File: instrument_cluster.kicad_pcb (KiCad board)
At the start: 2 copper layers, 99.1 x 45.7 mm, 86 parts, among them J1 Conn_02x16_Top_Bottom, J2 Conn_02x16_Top_Bottom, J3 USB mini-B SMD, J4 NOT_FITTED_SWD_Conn_01x04_Male, J5 54819-0572, J6 NOT_FITTED_SWD_Conn_01x04_Male, U1 LM2575S-5.0_NOPB, U10 74HC4050D, U11 TJA1040T, U12 TJA1040T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

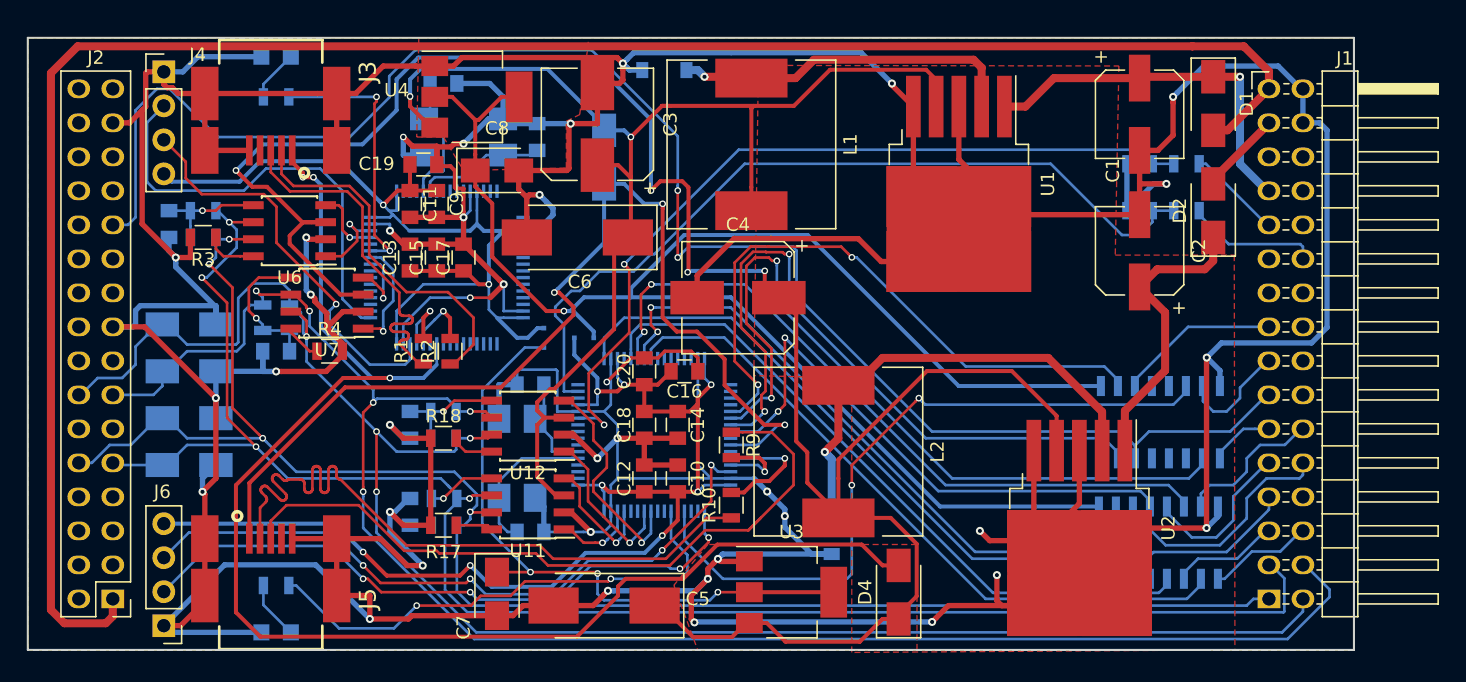
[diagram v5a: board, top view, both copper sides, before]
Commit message: fix USB footprint
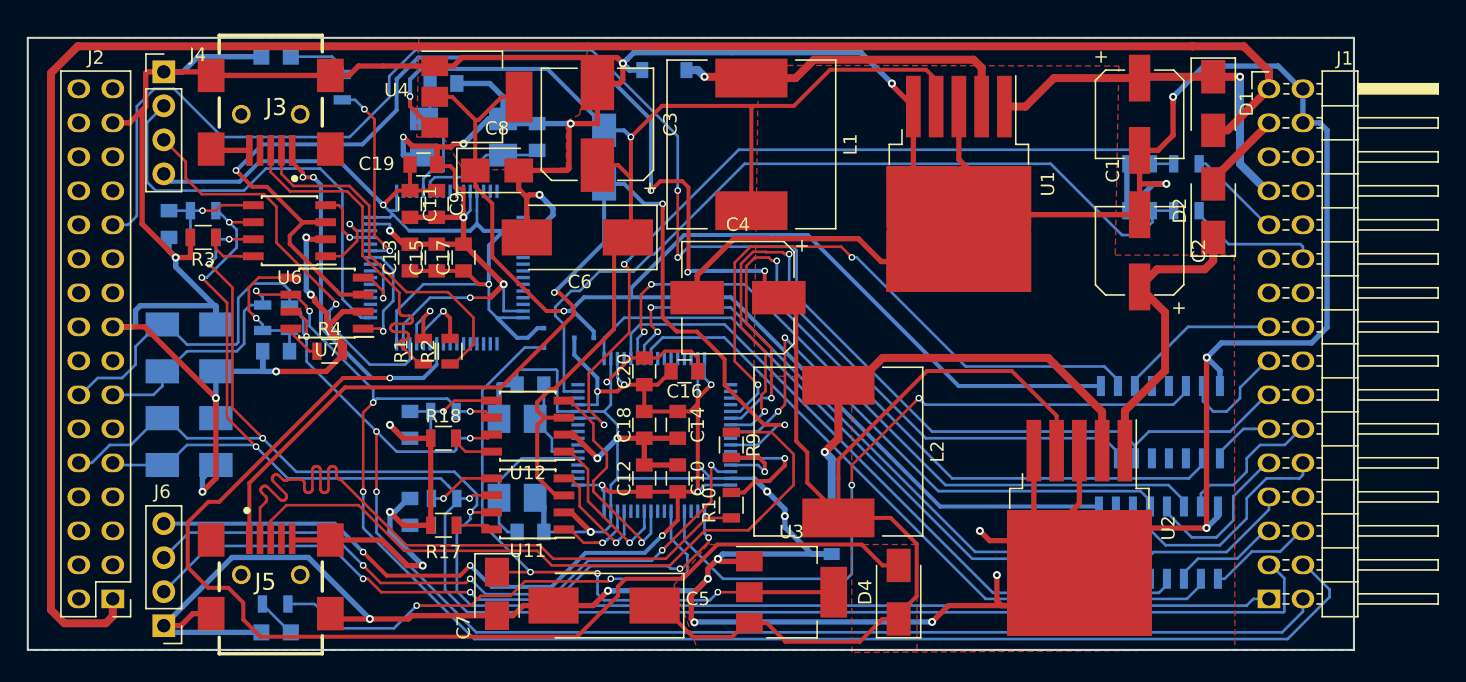
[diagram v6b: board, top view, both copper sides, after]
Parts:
- J3: value USB mini-B SMD -> USB mini-B; footprint zpkl:USB_mini_B -> zpkl:USB-B-M5-SMD-C
- J5: value 54819-0572 -> USB_mini_B; footprint zpkl:USB_mini_B -> zpkl:USB-B-M5-SMD-C
- moved J3 7.71 mm to (129.9, 84.9), turned to 180 degrees
- moved J5 7.71 mm to (122.2, 131.1), turned to 0 degrees
- moved R15 5.00 mm to (131.4, 88.8), turned to 270 degrees
- moved R16 1.38 mm to (126.4, 127.4)
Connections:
- net Net-(J5-Pad2) renamed /Module B (2can_filter+extra)/module_b_usb_D-
- net Net-(J5-Pad3) renamed /Module B (2can_filter+extra)/module_b_usb_D+
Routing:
- net GND: track 692.9 -> 669.7 mm
- net /Module A (2can_filter)/led_1: track 20.0 -> 14.8 mm
- net /USB_Vbus-A: track 105.5 -> 109.9 mm
- net Net-(D14-Pad2): track 4.35 -> 3.02 mm
- net Net-(D13-Pad2): track 3.85 -> 4.72 mm
- net /Module B (2can_filter+extra)/led_2: track 37.9 -> 37.4 mm
